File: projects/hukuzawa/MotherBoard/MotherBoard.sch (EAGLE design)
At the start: 0 parts

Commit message: マザーボード完成
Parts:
- added BATTLINE, MULTISUPPA, MULTISUPPB, RXPORT, TXPORT: 3X1A, 3M_372xx:3X1A
- added C1, C2: 47uF, FP-21T for MITS:CPOL-EU2-5MM
- added C3: C0.1UF, FP-21T for MITS:C0.1UF
- added HOLE1, HOLE2, HOLE3, HOLE4: HOLE3.3M3BOLT, FP-21T for MITS:HOLE3.3M3BOLT
- added I2CPORT, MULTIPORTA, MULTIPORTB: 4X2, 3M_372xx:4X2
- added IC1: PIC16F886, PIC:PIC16F886
- added LED1, LED2, LED3, LED4: (no value), FP-21T for MITS:LED5MM
- added NJM1: NJM7805, My_NJM7805:NJM7805
- added Q1: CERALOCK, FP-21T for MITS:CERALOCK
- added R1, R2, R3, R4: 1k, rcl:R-EU_R3216W
- added S1: (no value), switch:SLIDESW
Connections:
- new net +5V: C2.+, C3.1, IC1.VDD, NJM1.OUT
- new net 9VLINE: BATTLINE-1.S, S1.2
- new net A0: IC1.RA0/AN0/ULPWU/C12IN0-, MULTIPORTA1-1.S
- new net A1: IC1.RA1/AN1/C12IN1-, MULTIPORTA1-2.S
- new net A2: IC1.RA2/AN2/VREF-/CVREF/C2IN+, MULTIPORTA1-3.S
- new net A3: IC1.RA3/AN3/VREF+/C1IN+, MULTIPORTA1-4.S
- new net A4: IC1.RA4/TOCKI/C1OUT, MULTIPORTA2-1.S
- new net A5: IC1.RA5/AN4/!SS!/C2OUT, MULTIPORTA2-2.S
- new net A6: IC1.RA6/OSC2/CLKOUT, MULTIPORTA2-3.S, Q1.P$3
- new net A7: IC1.RA7/OSC1/CLKIN, MULTIPORTA2-4.S, Q1.P$1
- new net B0: IC1.RB0/AN12/INT, MULTIPORTB1-1.S
- new net B1: IC1.RB1/AN10/P1C/C12IN3-, MULTIPORTB1-2.S
- new net B2: IC1.RB2/AN8/P1B, MULTIPORTB1-3.S
- new net B3: IC1.RB3/AN9/PGM/C12IN2-, MULTIPORTB1-4.S
- new net B4: IC1.RB4/AN11/P1D, MULTIPORTB2-1.S
- new net B5: IC1.RB5/AN13/!T1G, MULTIPORTB2-2.S
- new net B6: IC1.RB6/ICSPCLK, MULTIPORTB2-3.S
- new net B7: IC1.RB7/ICSPDAT, MULTIPORTB2-4.S
- new net GND: BATTLINE-2.S, BATTLINE-3.S, C1.-, C2.-, C3.2, I2CPORT1-4.S, I2CPORT2-4.S, IC1.VSS1, IC1.VSS2, MULTISUPPA-2.S, MULTISUPPA-3.S, MULTISUPPB-2.S, MULTISUPPB-3.S, NJM1.GND, Q1.P$2, R1.2, R2.2, R3.2, R4.2, RXPORT-3.S, TXPORT-3.S
- new net LED0: IC1.RC0/T1OSO/T1CKI, LED1.A
- new net LED1: IC1.RC1/T1OSI/CCP2, LED2.A
- new net LED2: IC1.RC2/P1A/CCP1, LED3.A
- new net N$3: LED1.C, R1.1
- new net N$4: LED2.C, R2.1
- new net N$5: LED3.C, R3.1
- new net N$6: LED4.C, R4.1
- new net OPRLED: IC1.RC5/SDO, LED4.A
- new net RX: IC1.RC7/RX/DT, RXPORT-2.S
- new net SCL: I2CPORT1-2.S, I2CPORT2-2.S, IC1.RC3/SCK/SCL
- new net SDA: I2CPORT1-3.S, I2CPORT2-3.S, IC1.RC4/SDI/SDA
- new net TX: IC1.RC6/TX/CK, TXPORT-2.S
- new net V+: C1.+, I2CPORT1-1.S, I2CPORT2-1.S, MULTISUPPA-1.S, MULTISUPPB-1.S, NJM1.IN, RXPORT-1.S, S1.3, TXPORT-1.S
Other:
- note added: "2017/07/04"
- note added: "Mother Board"
- note added: "NIT,KC Robo"
- note added: "電源"

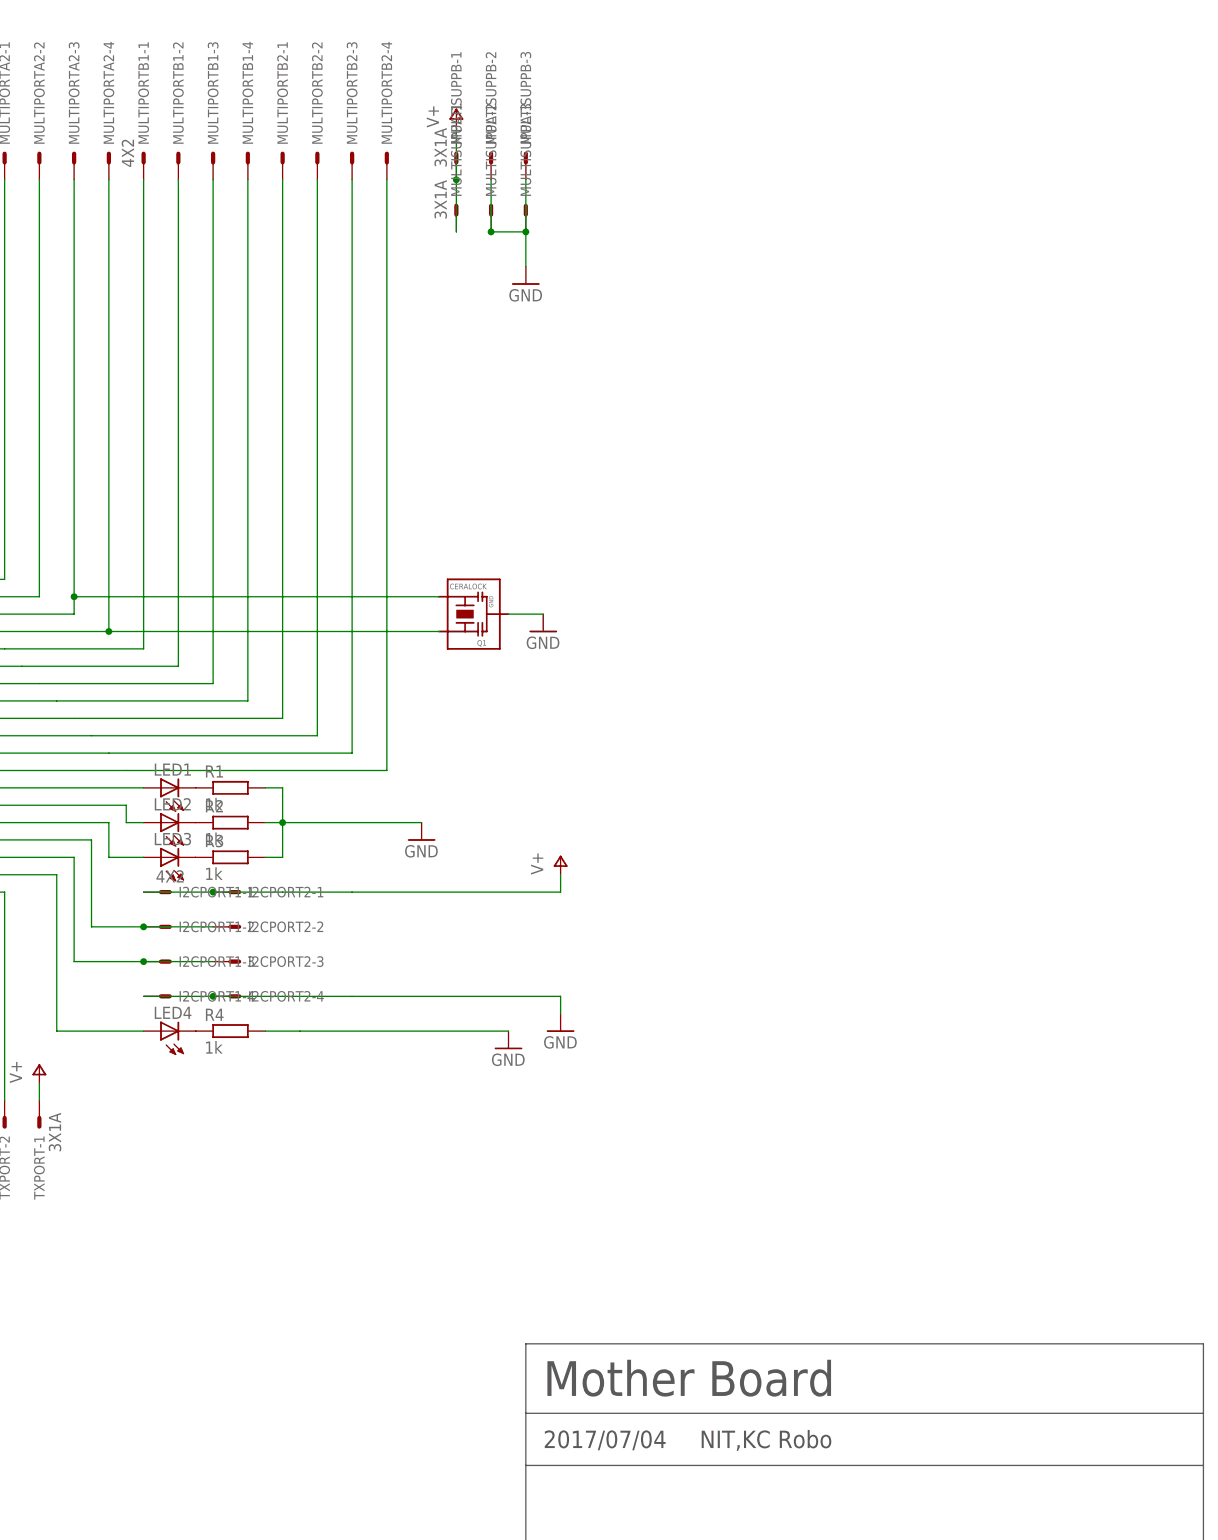
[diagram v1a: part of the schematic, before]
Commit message: マザーボード修正
一部文字の見えにくい部分を修正
PICのライブラリの重大な問題を修正
回路図・ボード図をpng,pdfにエクスポート
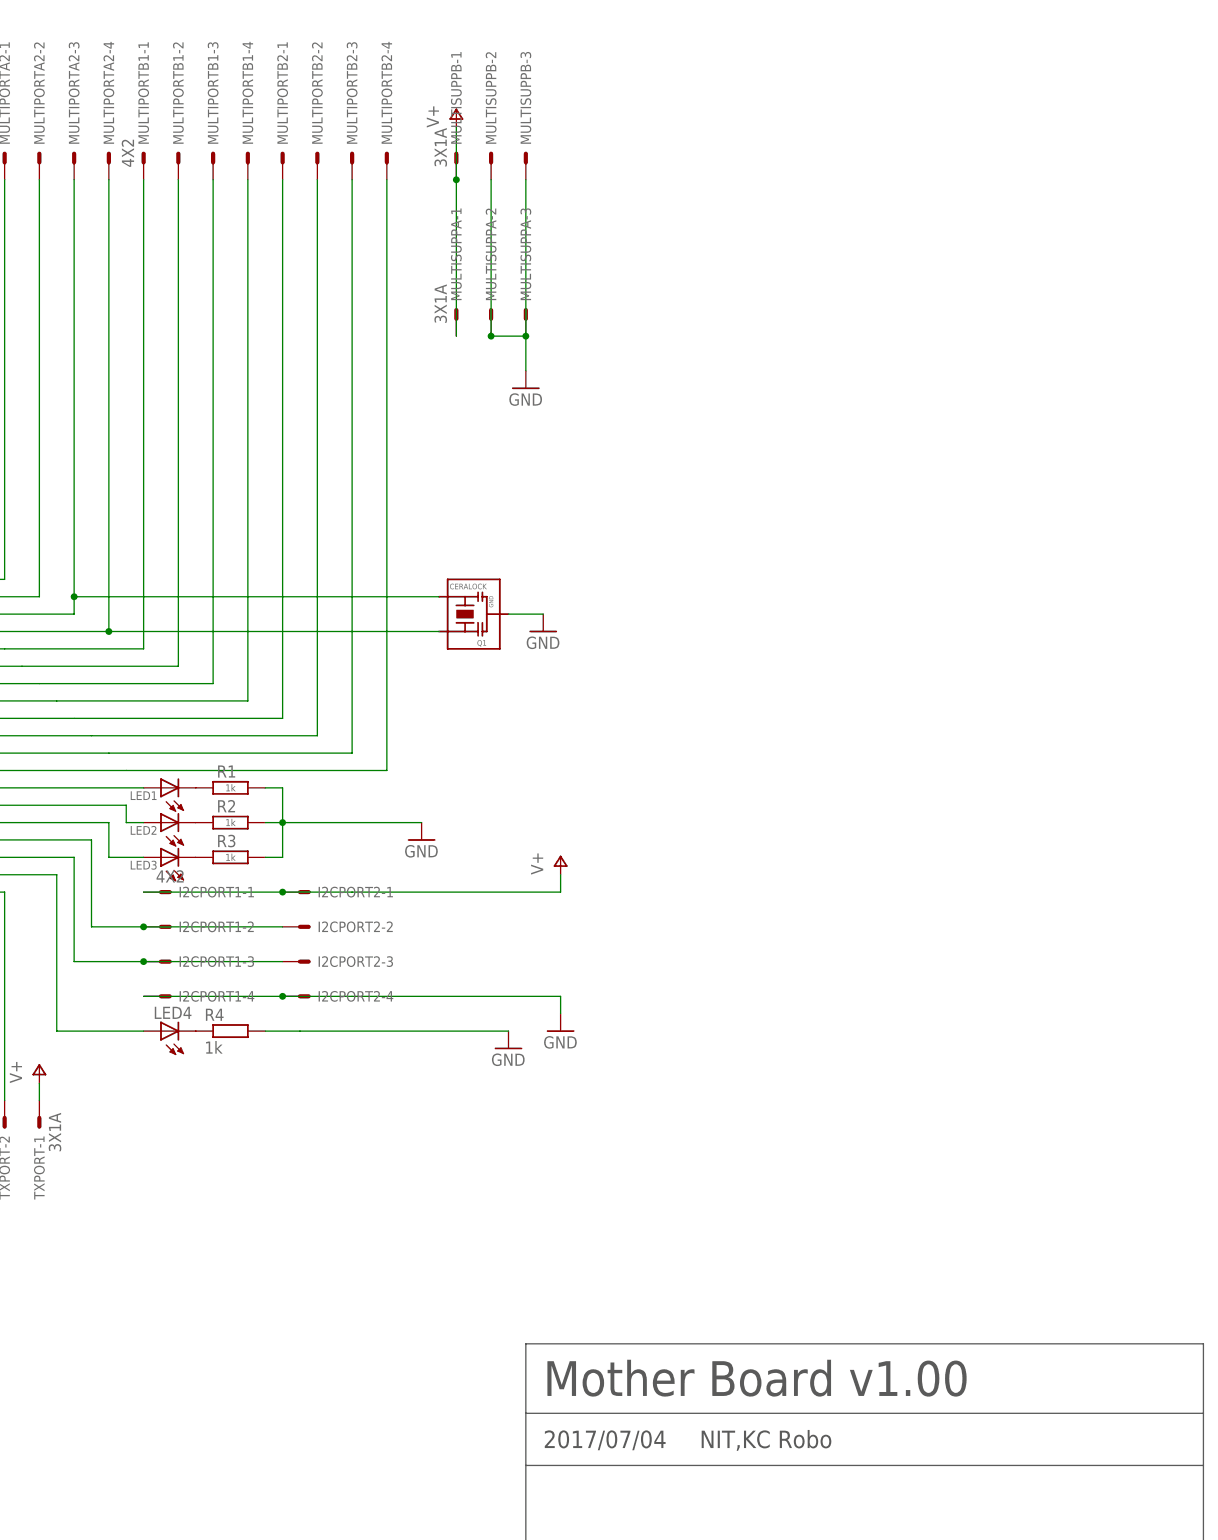
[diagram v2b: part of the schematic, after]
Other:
- note added: "Mother Board v1.00"
- note removed: "Mother Board"
- moved on the sheet: I2CPORT2-1, I2CPORT2-2, I2CPORT2-3, I2CPORT2-4, MULTISUPPA-1, MULTISUPPA-2, MULTISUPPA-3

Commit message: マザーボード修正
3.3mm穴がショートしないよう修正
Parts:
- HOLE1, HOLE2, HOLE3, HOLE4: device FP-21T for MITS:HOLE3.3M3BOLT -> Hole:HOLE3.3M3BOLT
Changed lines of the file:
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@@
 <part name="P+7" library="supply1" deviceset="V+" device=""/>
 <part name="GND8" library="supply1" deviceset="GND" device=""/>
-<part name="HOLE4" library="FP-21T for MITS" deviceset="HOLE3.3" device="M3BOLT"/>
-<part name="HOLE3" library="FP-21T for MITS" deviceset="HOLE3.3" device="M3BOLT"/>
-<part name="HOLE2" library="FP-21T for MITS" deviceset="HOLE3.3" device="M3BOLT"/>
-<part name="HOLE1" library="FP-21T for MITS" deviceset="HOLE3.3" device="M3BOLT"/>
 <part name="IC1" library="PIC" deviceset="PIC16F886" device=""/>
+<part name="HOLE4" library="Hole" deviceset="HOLE3.3" device="M3BOLT"/>
+<part name="HOLE3" library="Hole" deviceset="HOLE3.3" device="M3BOLT"/>
+<part name="HOLE2" library="Hole" deviceset="HOLE3.3" device="M3BOLT"/>
+<part name="HOLE1" library="Hole" deviceset="HOLE3.3" device="M3BOLT"/>
 </parts>
 <sheets>
@@
 <instance part="P+7" gate="1" x="88.9" y="106.68"/>
 <instance part="GND8" gate="1" x="99.06" y="66.04"/>
+<instance part="IC1" gate="IC" x="-25.4" y="17.78"/>
 <instance part="HOLE4" gate="G$1" x="-195.58" y="-119.38"/>
 <instance part="HOLE3" gate="G$1" x="-195.58" y="-114.3"/>
 <instance part="HOLE2" gate="G$1" x="-195.58" y="-109.22"/>
 <instance part="HOLE1" gate="G$1" x="-195.58" y="-104.14"/>
-<instance part="IC1" gate="IC" x="-25.4" y="17.78"/>
 </instances>
 <busses>

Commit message: マザーボード回路ver1.20
ポート部分仕様変更
再配置・再配線
回路基板サイズの縮小
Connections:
- removed net 9VLINE: BATTLINE-1.S, S1.2
- new net BATTLINE: BATTLINE-2.S, S1.3
- net GND: now also BATTLINE-1.S, I2CPORT1-1.S, I2CPORT2-1.S, MULTISUPPA-1.S, MULTISUPPB-1.S, RXPORT-1.S, S1.1, TXPORT-1.S; no longer BATTLINE-2.S, I2CPORT1-4.S, I2CPORT2-4.S, MULTISUPPA-2.S, MULTISUPPB-2.S, RXPORT-3.S, TXPORT-3.S
- net RX: now also RXPORT-3.S; no longer RXPORT-2.S
- net SCL: now also I2CPORT1-3.S, I2CPORT2-3.S; no longer I2CPORT1-2.S, I2CPORT2-2.S
- net SDA: now also I2CPORT1-4.S, I2CPORT2-4.S; no longer I2CPORT1-3.S, I2CPORT2-3.S
- net TX: now also TXPORT-3.S; no longer TXPORT-2.S
- net V+: now also I2CPORT1-2.S, I2CPORT2-2.S, MULTISUPPA-2.S, MULTISUPPB-2.S, RXPORT-2.S, S1.2, TXPORT-2.S; no longer I2CPORT1-1.S, I2CPORT2-1.S, MULTISUPPA-1.S, MULTISUPPB-1.S, RXPORT-1.S, S1.3, TXPORT-1.S
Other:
- note added: "2017/09/05"
- note added: "Mother Board v1.20"
- note removed: "2017/07/04"
- note removed: "Mother Board v1.00"
- moved on the sheet: BATTLINE-1, BATTLINE-2, I2CPORT1-1, I2CPORT1-2, I2CPORT1-3, I2CPORT1-4, I2CPORT2-1, I2CPORT2-2, I2CPORT2-3, I2CPORT2-4, IC1, LED1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

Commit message: マザーボード回路 v1.21
PICから外部に流す電源を制御するよう仕様変更
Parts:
- added TR1: 2SC1815, FP-21T for MITS:2SC1815
- R4: value 1k -> 10k
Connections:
- removed net OPRLED: IC1.RC5/SDO, LED4.A
- new net CTRLSUPP: I2CPORT1-2.S, I2CPORT2-2.S, LED4.A, MULTISUPPA-2.S, MULTISUPPB-2.S, RXPORT-2.S, TR1.E, TXPORT-2.S
- new net OPR: IC1.RC5/SDO, TR1.B
- net V+: now also TR1.C; no longer I2CPORT1-2.S, I2CPORT2-2.S, MULTISUPPA-2.S, MULTISUPPB-2.S, RXPORT-2.S, TXPORT-2.S
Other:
- note added: "Mother Board v1.21"
- note removed: "Mother Board v1.20"
- moved on the sheet: I2CPORT1-1, I2CPORT1-2, I2CPORT1-3, I2CPORT1-4, I2CPORT2-1, I2CPORT2-2, I2CPORT2-3, I2CPORT2-4, MULTISUPPA-1, MULTISUPPA-2, MULTISUPPA-3, MULTISUPPB-1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
